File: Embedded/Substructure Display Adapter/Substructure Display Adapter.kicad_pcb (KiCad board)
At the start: 2 copper layers, 29 x 30 mm, 9 parts, among them J1 HUB75, J2 Input, J3 Output, U1 D0 FFC, U2 74HC245D_653, U3 74HC245D_653

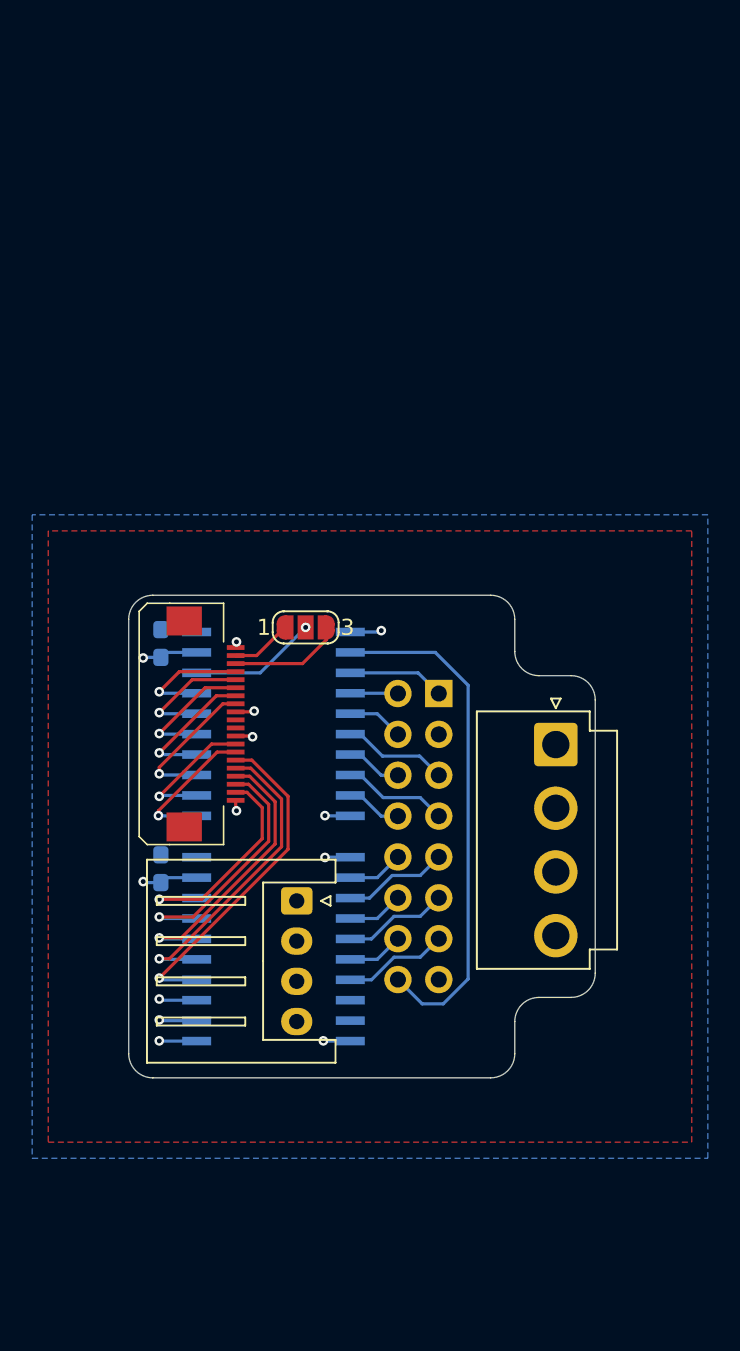
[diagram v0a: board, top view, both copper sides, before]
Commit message: Added Component placement ideation
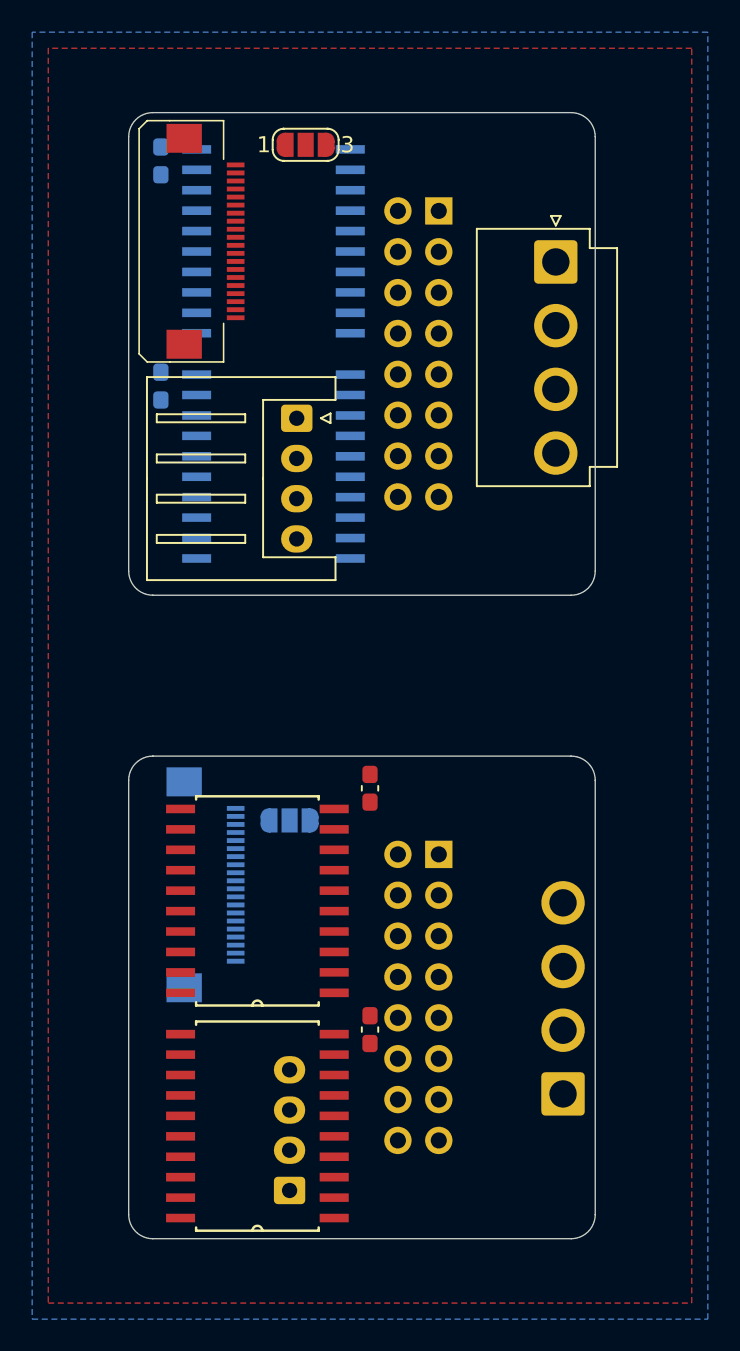
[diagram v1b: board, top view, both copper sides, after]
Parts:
- added C3: 10uF, Capacitor_SMD:C_0603_1608Metric_Pad1.08x0.95mm_HandSolder, F.Cu at (121.0, 67.0)
- added C4: 10uF, Capacitor_SMD:C_0603_1608Metric_Pad1.08x0.95mm_HandSolder, F.Cu at (121.0, 82.0)
- added J4: HUB75, Connector_PinHeader_2.54mm:PinHeader_2x08_P2.54mm_Vertical, B.Cu at (125.3, 71.1)
- added J5: Input, Connector_JST:JST_XH_S4B-XH-A_1x04_P2.50mm_Horizontal, B.Cu at (116.0, 92.0)
- added J6: Output, Connector_JST:JST_VH_B4P-VH-B_1x04_P3.96mm_Vertical, B.Cu at (133.0, 86.0)
- added JP2: SolderJumper_3_Open, Jumper:SolderJumper-3_P1.3mm_Open_RoundedPad1.0x1.5mm_NumberLabels, B.Cu at (116.0, 69.0)
- added U4: D0 FFC, FCC:FFC 0.8mm 20P, B.Cu at (112.0, 73.0)
- added U5: 74HC245D_653, 74HC245:SOIC127P1032X265-20N, F.Cu at (114.0, 88.0)
- added U6: 74HC245D_653, 74HC245:SOIC127P1032X265-20N, F.Cu at (114.0, 74.0)
- moved C1 30.0 mm to (108.0, 28.0)
- moved C2 30.0 mm to (108.0, 42.0)
- moved J1 30.0 mm to (125.3, 31.1)
- moved J2 30.0 mm to (116.4, 44.0)
- moved J3 30.0 mm to (132.6, 34.3)
- moved JP1 30.0 mm to (117.0, 27.0)
- moved U1 30.0 mm to (112.0, 33.0)
- moved U2 30.0 mm to (115.0, 33.0)
- moved U3 30.0 mm to (115.0, 47.0)
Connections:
- JP1 pad 1: Disp GPIO 0 -> Disp GPIO 7
- JP1 pad 3: Disp GPIO 1 -> Disp GPIO 8
- U2 pad 11: Disp GPIO 10 -> Disp GPIO 6
- U2 pad 12: Disp GPIO 9 -> Disp GPIO 5
- U2 pad 13: Disp GPIO 6 -> Disp GPIO 4
- U2 pad 14: Disp GPIO 5 -> Disp GPIO 3
- U2 pad 15: Disp GPIO 4 -> Disp GPIO 2
- U2 pad 16: Disp GPIO 3 -> Disp GPIO 1
- U2 pad 17: Disp GPIO 2 -> Disp GPIO 0
- U3 pad 13: unconnected-(U3-B5-Pad13) -> Disp GPIO 9
- U3 pad 14: Disp GPIO 11 -> Disp GPIO 10
- U3 pad 15: Disp GPIO 12 -> Disp GPIO 11
- U3 pad 16: Disp GPIO 13 -> Disp GPIO 12
- U3 pad 17: Disp GPIO 14 -> Disp GPIO 13
- U3 pad 18: Disp GPIO 15 -> Disp GPIO 14
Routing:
- net OE: track 32.1 -> 0.00 mm
- net Disp GPIO 11: track 21.2 -> 0.00 mm, vias 1 -> 0
- net Disp GPIO 12: track 19.4 -> 0.00 mm, vias 1 -> 0
- net Disp GPIO 13: track 17.7 -> 0.00 mm, vias 1 -> 0
- net Disp GPIO 14: track 16.0 -> 0.00 mm, vias 1 -> 0
- net GND: track 14.8 -> 0.00 mm, vias 8 -> 0
- net Disp GPIO 15: track 14.3 -> 0.00 mm, vias 1 -> 0
- net Disp GPIO 6: track 9.14 -> 0.00 mm, vias 1 -> 0
- net Disp GPIO 10: track 8.99 -> 0.00 mm, vias 1 -> 0
- net Disp GPIO 5: track 8.59 -> 0.00 mm, vias 1 -> 0
- net Disp GPIO 9: track 8.44 -> 0.00 mm, vias 1 -> 0
- net Disp GPIO 4: track 8.27 -> 0.00 mm, vias 1 -> 0
- net Disp GPIO 3: track 7.95 -> 0.00 mm, vias 1 -> 0
- net Disp Display Select: track 7.95 -> 0.00 mm, vias 1 -> 0
- net Disp GPIO 2: track 7.63 -> 0.00 mm, vias 1 -> 0
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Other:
- board size 29 x 30 mm -> 29 x 70 mm

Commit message: Added Routing for right adapter
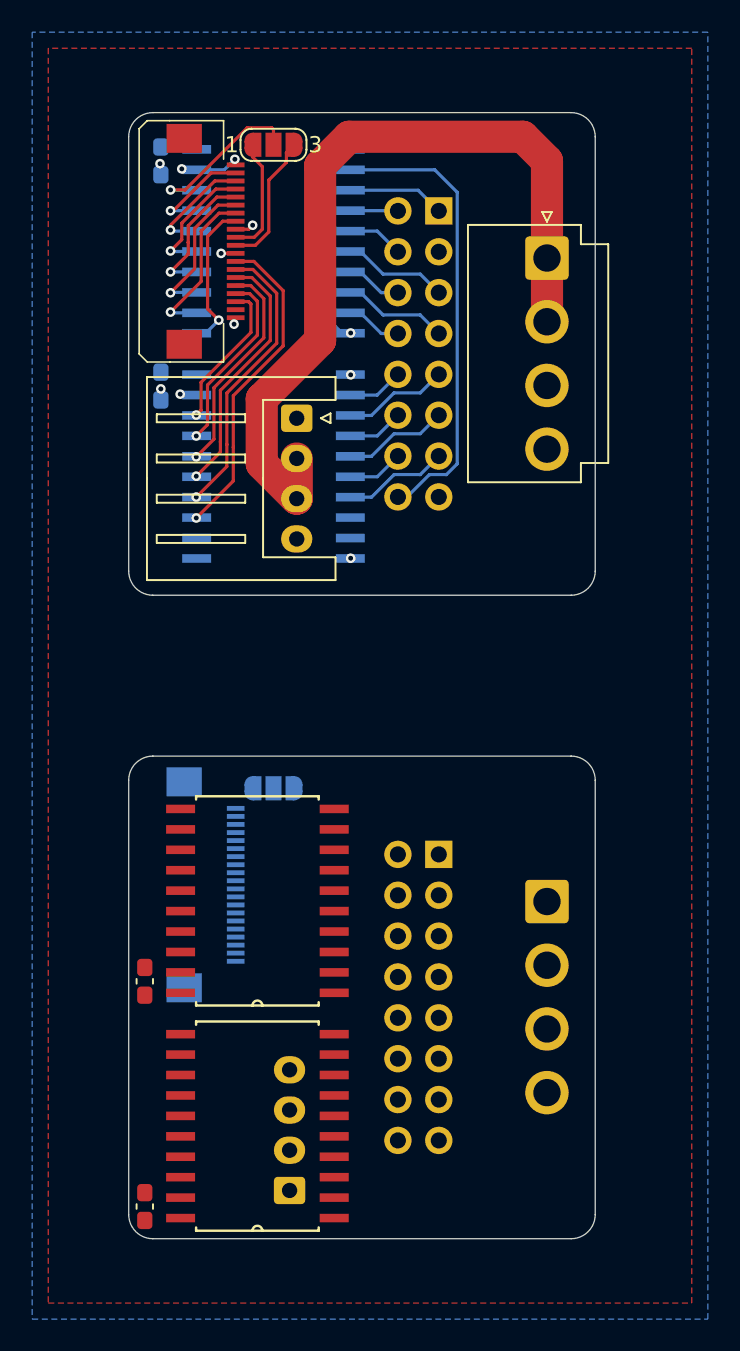
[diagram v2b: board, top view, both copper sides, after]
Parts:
- moved C3 18.4 mm to (107.0, 79.0), turned to 90 degrees
- moved C4 17.8 mm to (107.0, 93.0), turned to 90 degrees
- moved U5 14.0 mm to (114.0, 74.0)
- moved U6 14.0 mm to (114.0, 88.0)
- moved J6 12.0 mm to (132.0, 74.0), turned to -90 degrees
- moved JP2 2.24 mm to (115.0, 67.0)
- moved JP1 2.00 mm to (115.0, 27.0)
- moved J3 0.60 mm to (132.0, 34.0)
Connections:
- U4 pad 10: Alt Disp GPIO 7 -> Alt Disp GPIO 8
- U4 pad 11: Alt Disp GPIO 8 -> Alt Disp GPIO 7
- U4 pad 13: Alt Disp GPIO 9 -> Alt Disp GPIO 6
- U4 pad 14: Alt Disp GPIO 10 -> Alt Disp GPIO 5
- U4 pad 15: Alt Disp GPIO 11 -> Alt Disp GPIO 4
- U4 pad 16: Alt Disp GPIO 12 -> Alt Disp GPIO 3
- U4 pad 17: Alt Disp GPIO 13 -> Alt Disp GPIO 2
- U4 pad 18: Alt Disp GPIO 14 -> Alt Disp GPIO 1
- U4 pad 19: Alt Disp GPIO 15 -> Alt Disp GPIO 0
- U4 pad 2: Alt Disp GPIO 0 -> Alt Disp GPIO 15
- U4 pad 3: Alt Disp GPIO 1 -> Alt Disp GPIO 14
- U4 pad 4: Alt Disp GPIO 2 -> Alt Disp GPIO 13
- U4 pad 5: Alt Disp GPIO 3 -> Alt Disp GPIO 12
- U4 pad 6: Alt Disp GPIO 4 -> Alt Disp GPIO 11
- U4 pad 7: Alt Disp GPIO 5 -> Alt Disp GPIO 10
- U4 pad 8: Alt Disp GPIO 6 -> Alt Disp GPIO 9
- U5 pad 11: Alt Disp GPIO 6 -> Alt Disp Display Select
- U5 pad 12: Alt Disp GPIO 5 -> Alt Disp GPIO 0
- U5 pad 13: Alt Disp GPIO 4 -> Alt Disp GPIO 1
- U5 pad 14: Alt Disp GPIO 3 -> Alt Disp GPIO 2
- U5 pad 15: Alt Disp GPIO 2 -> Alt Disp GPIO 3
- U5 pad 16: Alt Disp GPIO 1 -> Alt Disp GPIO 4
- U5 pad 17: Alt Disp GPIO 0 -> Alt Disp GPIO 5
- U5 pad 18: Alt Disp Display Select -> Alt Disp GPIO 6
- U6 pad 11: unconnected-(U6-B7-Pad11) -> Alt Disp GPIO 14
- U6 pad 12: unconnected-(U6-B6-Pad12) -> Alt Disp GPIO 13
- U6 pad 13: Alt Disp GPIO 9 -> Alt Disp GPIO 12
- U6 pad 14: Alt Disp GPIO 10 -> Alt Disp GPIO 11
- U6 pad 15: Alt Disp GPIO 11 -> Alt Disp GPIO 10
- U6 pad 16: Alt Disp GPIO 12 -> Alt Disp GPIO 9
- U6 pad 17: Alt Disp GPIO 13 -> unconnected-(U6-B1-Pad17)
- U6 pad 18: Alt Disp GPIO 14 -> unconnected-(U6-B0-Pad18)
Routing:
- net +5V: track 0.00 -> 53.1 mm, vias 0 -> 2
- net OE: track 0.00 -> 28.6 mm
- net Disp GPIO 9: track 0.00 -> 20.1 mm, vias 0 -> 1
- net GND: track 0.00 -> 20.0 mm, vias 0 -> 9
- net Disp GPIO 10: track 0.00 -> 17.9 mm, vias 0 -> 1
- net Disp GPIO 11: track 0.00 -> 15.8 mm, vias 0 -> 1
- net Disp GPIO 12: track 0.00 -> 13.7 mm, vias 0 -> 1
- net Disp GPIO 13: track 0.00 -> 11.5 mm, vias 0 -> 1
- net Disp Display Select: track 0.00 -> 10.6 mm, vias 0 -> 1
- net Disp GPIO 5: track 0.00 -> 10.1 mm, vias 0 -> 1
- net Disp GPIO 4: track 0.00 -> 9.41 mm, vias 0 -> 1
- net Disp GPIO 14: track 0.00 -> 9.36 mm, vias 0 -> 1
- net Disp GPIO 6: track 0.00 -> 9.34 mm, vias 0 -> 1
- net Disp GPIO 3: track 0.00 -> 8.64 mm, vias 0 -> 1
- net Disp GPIO 8: track 0.00 -> 8.48 mm
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
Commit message: Added Routing for left adapter
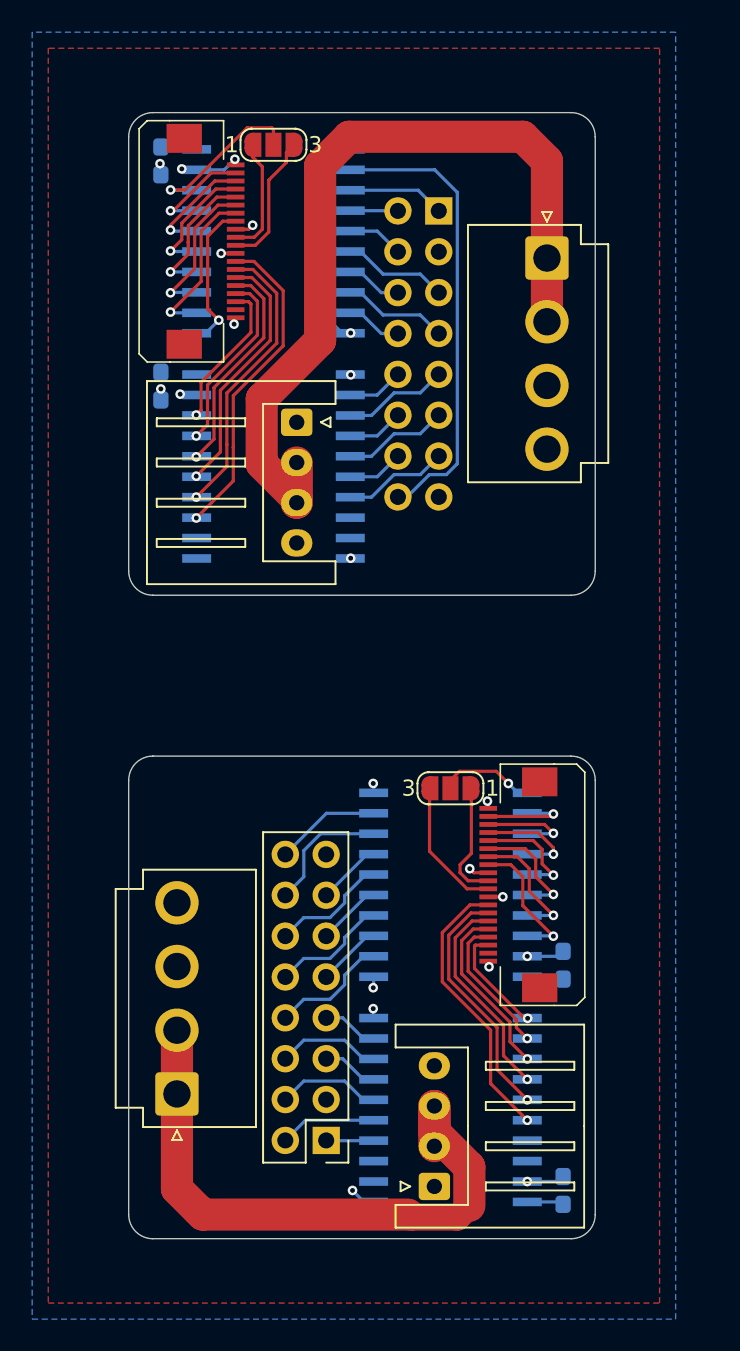
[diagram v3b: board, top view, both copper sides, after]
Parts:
- C3, C4, U5, U6: moved to B.Cu
- J4, J5, J6, JP2, U4: moved to F.Cu
- moved C3 26.0 mm to (133.0, 78.0)
- moved C4 26.0 mm to (133.0, 92.0)
- moved J6 25.9 mm to (109.0, 86.0), turned to 90 degrees
- moved J4 19.1 mm to (118.3, 88.9)
- moved U4 17.0 mm to (129.0, 73.0)
- moved U5 12.0 mm to (126.0, 73.0), turned to 0 degrees
- moved U6 12.0 mm to (126.0, 87.0), turned to 0 degrees
- moved JP2 11.0 mm to (126.0, 67.0), turned to 180 degrees
- moved J5 9.00 mm to (125.0, 91.8)
- moved J2 0.25 mm to (116.4, 44.2)
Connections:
- U5 pad 2: unconnected-(U5-A0-Pad2) -> Alt B1
- U5 pad 3: unconnected-(U5-A1-Pad3) -> Alt B
- U5 pad 4: unconnected-(U5-A2-Pad4) -> Alt A
- U5 pad 5: unconnected-(U5-A3-Pad5) -> Alt D
- U5 pad 6: unconnected-(U5-A4-Pad6) -> Alt C
- U5 pad 7: unconnected-(U5-A5-Pad7) -> Alt LAT
- U5 pad 8: unconnected-(U5-A6-Pad8) -> Alt CLK
- U5 pad 9: unconnected-(U5-A7-Pad9) -> Alt OE
- U6 pad 4: unconnected-(U6-A2-Pad4) -> Alt G0
- U6 pad 5: unconnected-(U6-A3-Pad5) -> Alt R0
- U6 pad 6: unconnected-(U6-A4-Pad6) -> Alt B0
- U6 pad 7: unconnected-(U6-A5-Pad7) -> Alt G1
- U6 pad 8: unconnected-(U6-A6-Pad8) -> Alt R1
- U6 pad 9: unconnected-(U6-A7-Pad9) -> Alt E
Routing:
- net +5V: track 53.1 -> 98.8 mm, vias 2 -> 4
- net Alt Disp GPIO 9: track 0.00 -> 17.4 mm, vias 0 -> 1
- net Alt Disp GPIO 10: track 0.00 -> 15.3 mm, vias 0 -> 1
- net Alt Disp GPIO 11: track 0.00 -> 13.1 mm, vias 0 -> 1
- net Alt Disp GPIO 12: track 0.00 -> 11.0 mm, vias 0 -> 1
- net GND: track 20.0 -> 29.0 mm, vias 9 -> 17
- net Alt Disp GPIO 13: track 0.00 -> 8.86 mm, vias 0 -> 1
- net Alt Disp GPIO 6: track 0.00 -> 8.57 mm, vias 0 -> 1
- net Alt Disp GPIO 8: track 0.00 -> 8.53 mm
- net Alt CLK: track 0.00 -> 8.03 mm
- net Alt Disp GPIO 5: track 0.00 -> 8.01 mm, vias 0 -> 1
- net Alt Disp GPIO 4: track 0.00 -> 7.51 mm, vias 0 -> 1
- net Alt Disp GPIO 7: track 0.00 -> 7.50 mm
- net Alt B1: track 0.00 -> 7.42 mm
- net Alt C: track 0.00 -> 7.34 mm
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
